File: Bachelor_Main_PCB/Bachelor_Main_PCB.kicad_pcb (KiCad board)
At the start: 2 copper layers, 9 parts, among them J1 F32Q-1A7H1-11022, U1 SC0683, U2 RC7620_1104625, U3 STM32H7A3ZITxQ

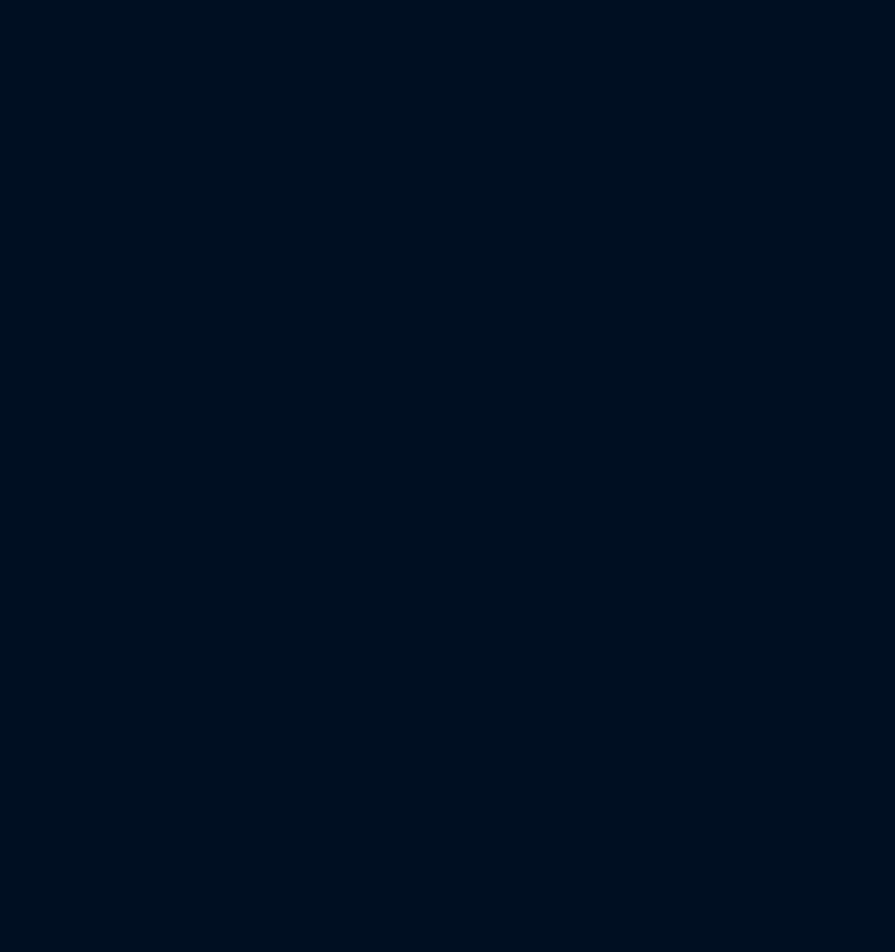
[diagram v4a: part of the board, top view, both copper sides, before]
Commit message: Add USB-Tranciever
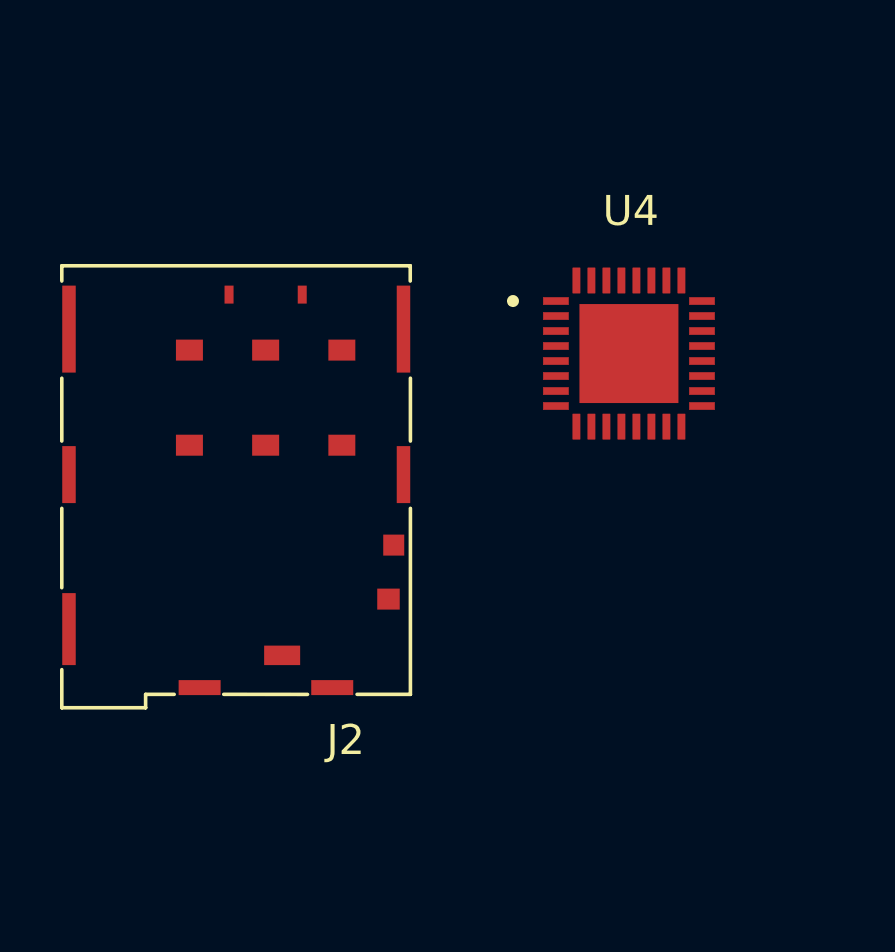
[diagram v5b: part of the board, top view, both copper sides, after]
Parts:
- added J2: JAE_SIM_Card_SF72S006, Connector_JAE:JAE_SIM_Card_SF72S006, F.Cu at (75.1, 58.4)
- added U4: USB3320C-EZK-TR, USB3320C-EZK-TR:QFN50P500X500X100-33N, F.Cu at (87.2, 56.1)

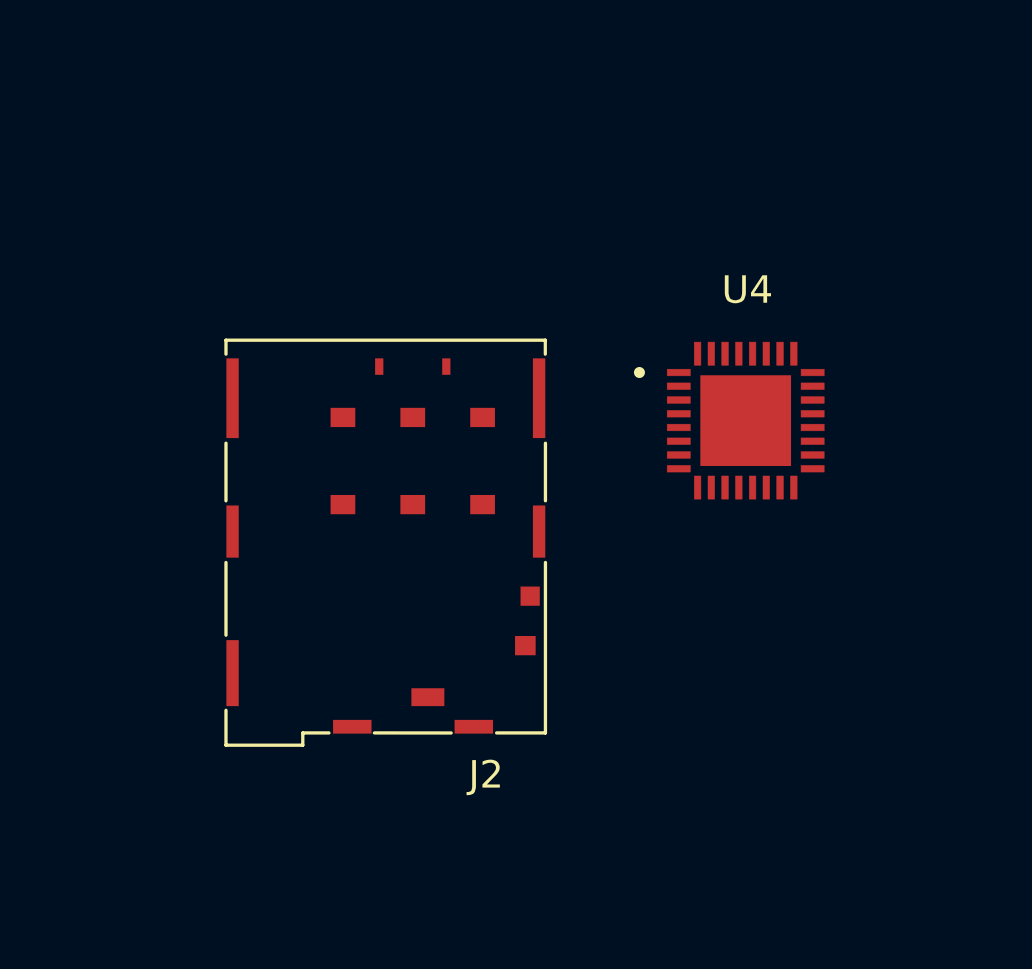
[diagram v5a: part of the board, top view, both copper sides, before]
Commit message: Add Y1 oscillator to the USB3320
24Mhz oscillator for the USB tranciever
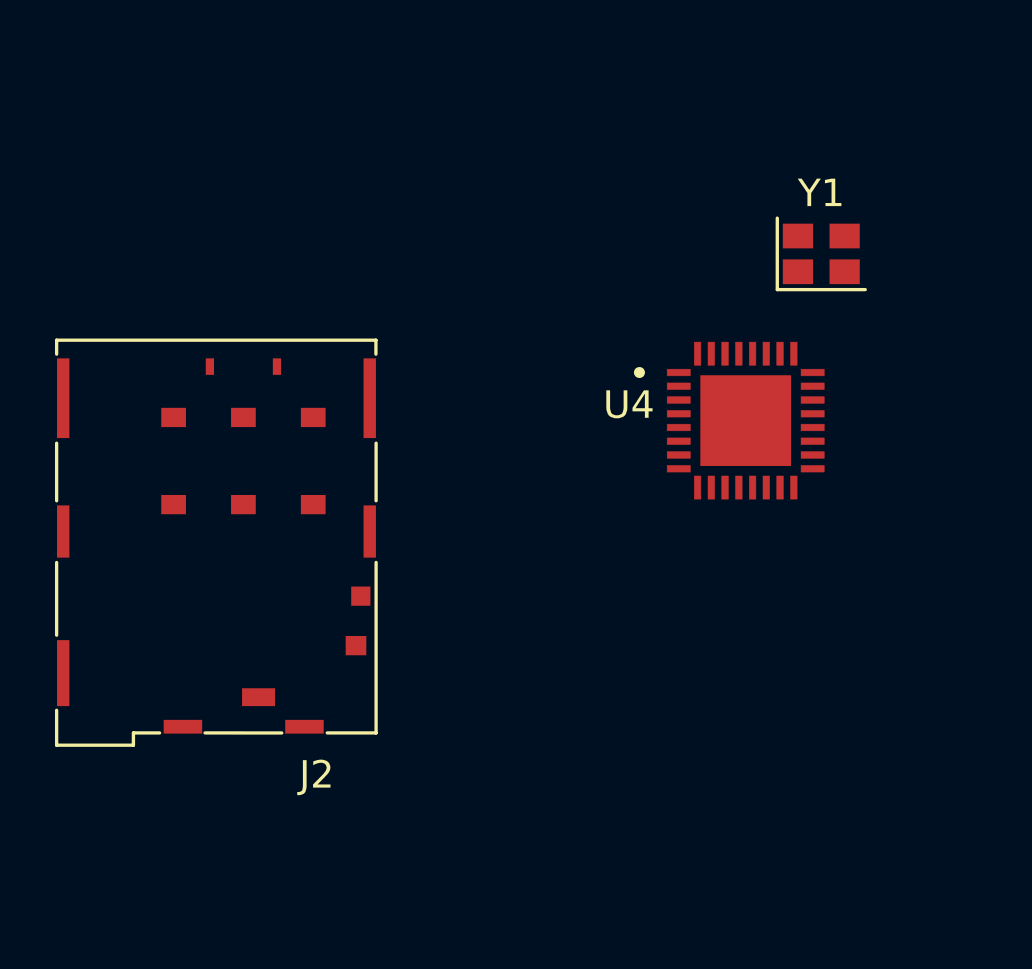
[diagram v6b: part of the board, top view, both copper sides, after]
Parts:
- added Y1: SG-210STF 24Mhz, Oscillator:Oscillator_SMD_SeikoEpson_SG210-4Pin_2.5x2.0mm, F.Cu at (90.0, 50.0)
- moved J2 6.16 mm to (69.0, 58.4)
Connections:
- U3 pad 134: unconnected-(U3-PB7-Pad134) -> USB_ULPI_data_7
- U3 pad 28: unconnected-(U3-PC0-Pad28) -> USB_ULPI_STP
- U3 pad 30: unconnected-(U3-PC2_C-Pad30) -> USB_ULPI_DIR
- U3 pad 31: unconnected-(U3-PC3_C-Pad31) -> USB_ULPI_NXT
- U3 pad 40: unconnected-(U3-PA3-Pad40) -> USB_ULPI_data_0
- U3 pad 44: unconnected-(U3-PA5-Pad44) -> USB_ULPI_CLK
- U3 pad 49: unconnected-(U3-PB0-Pad49) -> USB_ULPI_data_1
- U3 pad 50: unconnected-(U3-PB1-Pad50) -> USB_ULPI_data_2
- U3 pad 66: unconnected-(U3-PB10-Pad66) -> USB_ULPI_data_3
- U3 pad 67: unconnected-(U3-PB11-Pad67) -> USB_ULPI_data_4
- U3 pad 72: unconnected-(U3-PB12-Pad72) -> USB_ULPI_data_5
- U3 pad 73: unconnected-(U3-PB13-Pad73) -> USB_ULPI_data_6
- U4 pad 1: unconnected-(U4-CLKOUT-Pad1) -> USB_ULPI_CLK
- U4 pad 10: unconnected-(U4-DATA6-Pad10) -> USB_ULPI_data_6
- U4 pad 11: unconnected-(U4-REFSEL1-Pad11) -> Net-(U4-REFSEL0)
- U4 pad 13: unconnected-(U4-DATA7-Pad13) -> USB_ULPI_data_7
- U4 pad 14: unconnected-(U4-REFSEL2-Pad14) -> Net-(U4-REFSEL0)
- U4 pad 2: unconnected-(U4-NXT-Pad2) -> USB_ULPI_NXT
- U4 pad 26: unconnected-(U4-REFCLK-Pad26) -> Net-(U4-REFCLK)
- U4 pad 29: unconnected-(U4-STP-Pad29) -> USB_ULPI_STP
- U4 pad 3: unconnected-(U4-DATA0-Pad3) -> USB_ULPI_data_0
- U4 pad 31: unconnected-(U4-DIR-Pad31) -> USB_ULPI_DIR
- U4 pad 4: unconnected-(U4-DATA1-Pad4) -> USB_ULPI_data_1
- U4 pad 5: unconnected-(U4-DATA2-Pad5) -> USB_ULPI_data_2
- U4 pad 6: unconnected-(U4-DATA3-Pad6) -> USB_ULPI_data_3
- U4 pad 7: unconnected-(U4-DATA4-Pad7) -> USB_ULPI_data_4
- U4 pad 8: unconnected-(U4-REFSEL0-Pad8) -> Net-(U4-REFSEL0)
- U4 pad 9: unconnected-(U4-DATA5-Pad9) -> USB_ULPI_data_5

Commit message: Make correct stackup and add 90ohm differential pair usb
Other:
- copper layers 2 -> 4
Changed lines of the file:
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@@
 	(generator_version "9.0")
 	(general
-		(thickness 1.6)
+		(thickness 1.6062)
 		(legacy_teardrops no)
 	)
@@
 	(layers
 		(0 "F.Cu" signal)
+		(4 "In1.Cu" signal)
+		(6 "In2.Cu" signal)
 		(2 "B.Cu" signal)
 		(9 "F.Adhes" user "F.Adhesive")
@@
 	)
 	(setup
+		(stackup
+			(layer "F.SilkS"
+				(type "Top Silk Screen")
+				(color "White")
+			)
+			(layer "F.Paste"
+				(type "Top Solder Paste")
+			)
+			(layer "F.Mask"
+				(type "Top Solder Mask")
+				(color "Green")
+				(thickness 0.01)
+			)
+			(layer "F.Cu"
+				(type "copper")
+				(thickness 0.035)
+			)
+			(layer "dielectric 1"
+				(type "prepreg")
+				(thickness 0.2104)
+				(material "FR4")
+				(epsilon_r 4.4)
+				(loss_tangent 0.02)
+			)
+			(layer "In1.Cu"
+				(type "copper")
+				(thickness 0.0152)
+			)
+			(layer "dielectric 2"
+				(type "core")
+				(thickness 1.065)
+				(material "FR4")
+				(epsilon_r 4.4)
+				(loss_tangent 0.02)
+			)
+			(layer "In2.Cu"
+				(type "copper")
+				(thickness 0.0152)
+			)
+			(layer "dielectric 3"
+				(type "prepreg")
+				(thickness 0.2104)
+				(material "FR4")
+				(epsilon_r 4.4)
+				(loss_tangent 0.02)
+			)
+			(layer "B.Cu"
+				(type "copper")
+				(thickness 0.035)
+			)
+			(layer "B.Mask"
+				(type "Bottom Solder Mask")
+				(color "Green")
+				(thickness 0.01)
+			)
+			(layer "B.Paste"
+				(type "Bottom Solder Paste")
+			)
+			(layer "B.SilkS"
+				(type "Bottom Silk Screen")
+				(color "White")
+			)
+			(copper_finish "None")
+			(dielectric_constraints no)
+		)
 		(pad_to_mask_clearance 0)
 		(allow_soldermask_bridges_in_footprints no)
